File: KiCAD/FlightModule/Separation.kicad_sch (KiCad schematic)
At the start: 14 parts, among them J2 SN3, J3 SN4, Q1 AO3400A, Q2 AO3400A

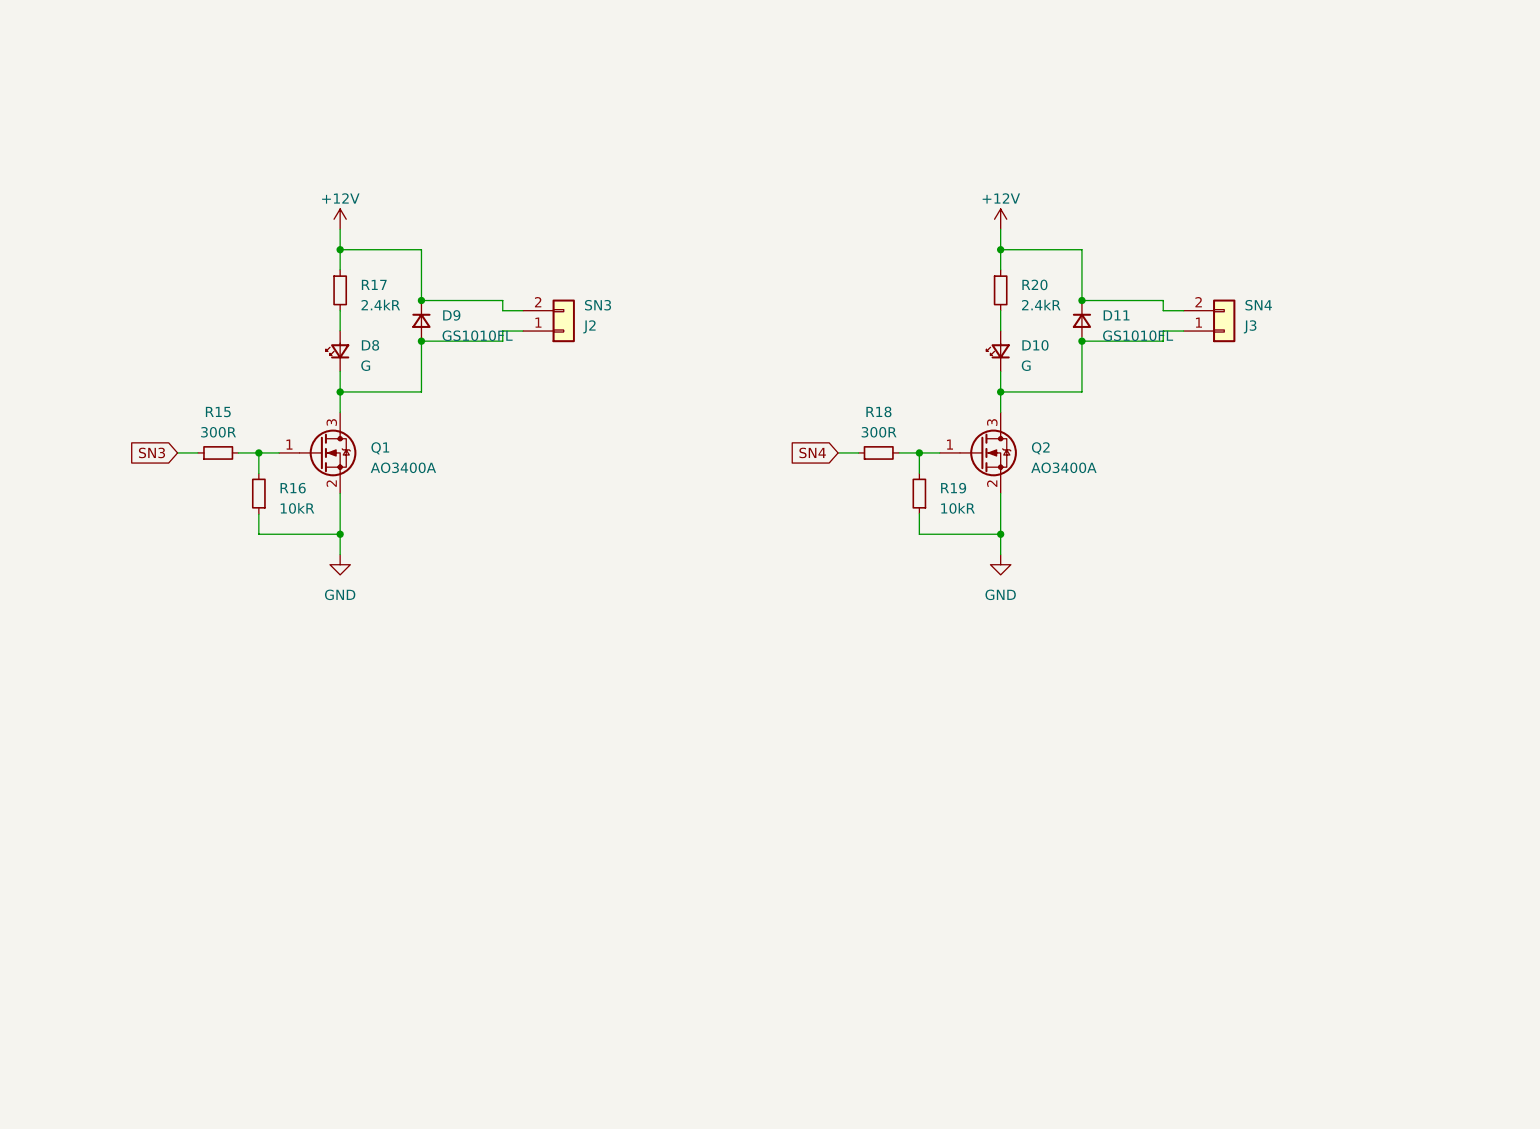
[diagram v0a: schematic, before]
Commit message: 分離周りの回路図完成
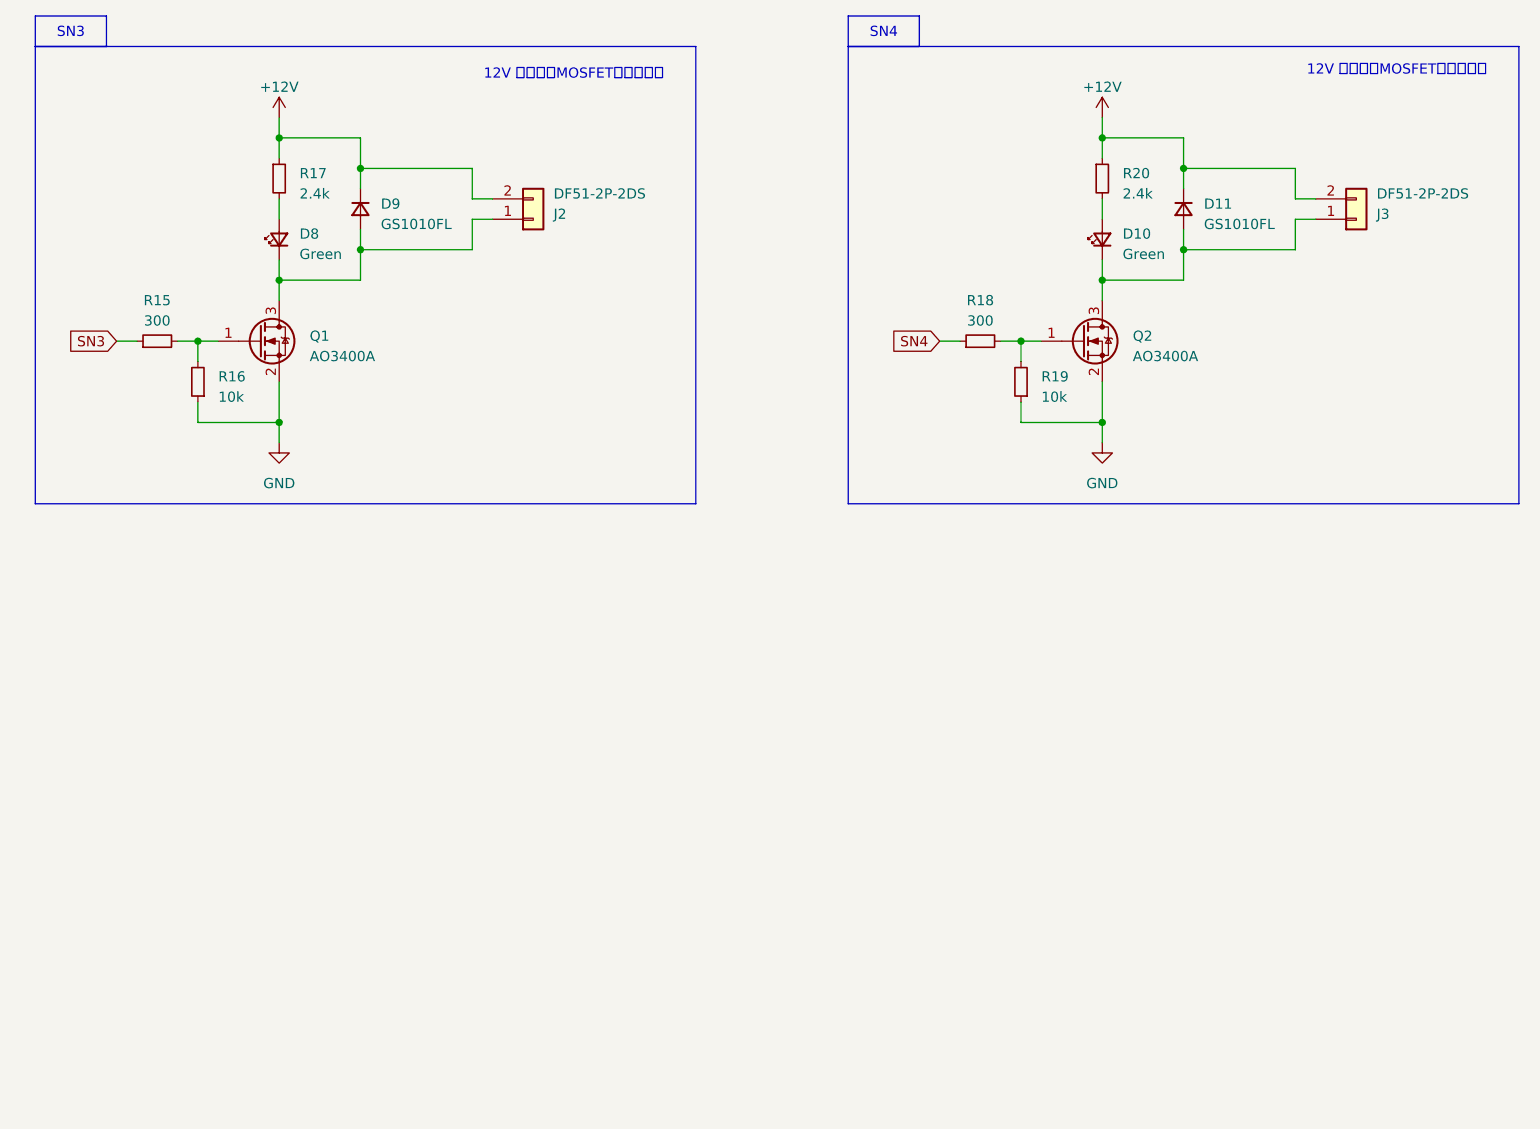
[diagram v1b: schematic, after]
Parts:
- D10, D8: value G -> Green
- J2: value SN3 -> DF51-2P-2DS; footprint Hirose_Connector:Hirose_DF1B -> TSRP_Connector_Hirose:DF51-2P-2DS
- J3: value SN4 -> DF51-2P-2DS; footprint Hirose_Connector:Hirose_DF1B -> TSRP_Connector_Hirose:DF51-2P-2DS
- R15, R18: value 300R -> 300
- R16, R19: value 10kR -> 10k
- R17, R20: value 2.4kR -> 2.4k
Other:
- note added: "12V ラインをMOSFETにより駆動"
- moved on the sheet: D10, D11, D8, D9, J2, J3, Q1, Q2, R15, R16, R17, R18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

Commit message: 配線8割り終わり．次の作業....
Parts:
- removed J2, J3: DF51-2P-2DS, TSRP_Connector_Hirose:DF51-2P-2DS, symbol Connector_Generic:Conn_01x02
- added J5: DF51A-4P-2DSA, TSRP_Connector_Hirose:DF51A-4P-2DSA, symbol Connector_Generic:Conn_01x04
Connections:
- net +12V: now also J5.2 (Pin_2), J5.4 (Pin_4)
- net at D10.1 (K), D11.2 (A), Q2.3 (D): now also J5.1 (Pin_1)
- net at D8.1 (K), D9.2 (A), Q1.3 (D): now also J5.3 (Pin_3)
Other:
- moved on the sheet: D10, D11, Q2, R18, R19, R20

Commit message: 最終確認終わり
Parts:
- R15, R18: value 300 -> 300R
- R16, R19: value 10k -> 10kR
- R17, R20: value 2.4k -> 2.4kR
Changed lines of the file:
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@@
 			)
 		)
-		(property "Value" "10k"
+		(property "Value" "10kR"
 			(at 48.26 69.215 0)
 			(effects
@@
 			)
 		)
-		(property "Value" "2.4k"
+		(property "Value" "2.4kR"
 			(at 58.42 43.815 0)
 			(effects
@@
 			)
 		)
-		(property "Value" "10k"
+		(property "Value" "10kR"
 			(at 49.53 145.415 0)
 			(effects
@@
 			)
 		)
-		(property "Value" "300"
+		(property "Value" "300R"
 			(at 40.64 59.69 90)
 			(effects
@@
 			)
 		)
-		(property "Value" "2.4k"
+		(property "Value" "2.4kR"
 			(at 59.69 120.015 0)
 			(effects
@@
 			)
 		)
-		(property "Value" "300"
+		(property "Value" "300R"
 			(at 41.91 135.89 90)
 			(effects
